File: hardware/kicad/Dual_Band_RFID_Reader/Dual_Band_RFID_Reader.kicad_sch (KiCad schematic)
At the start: 1 part, among them U1 Adafruit_Huzzah32

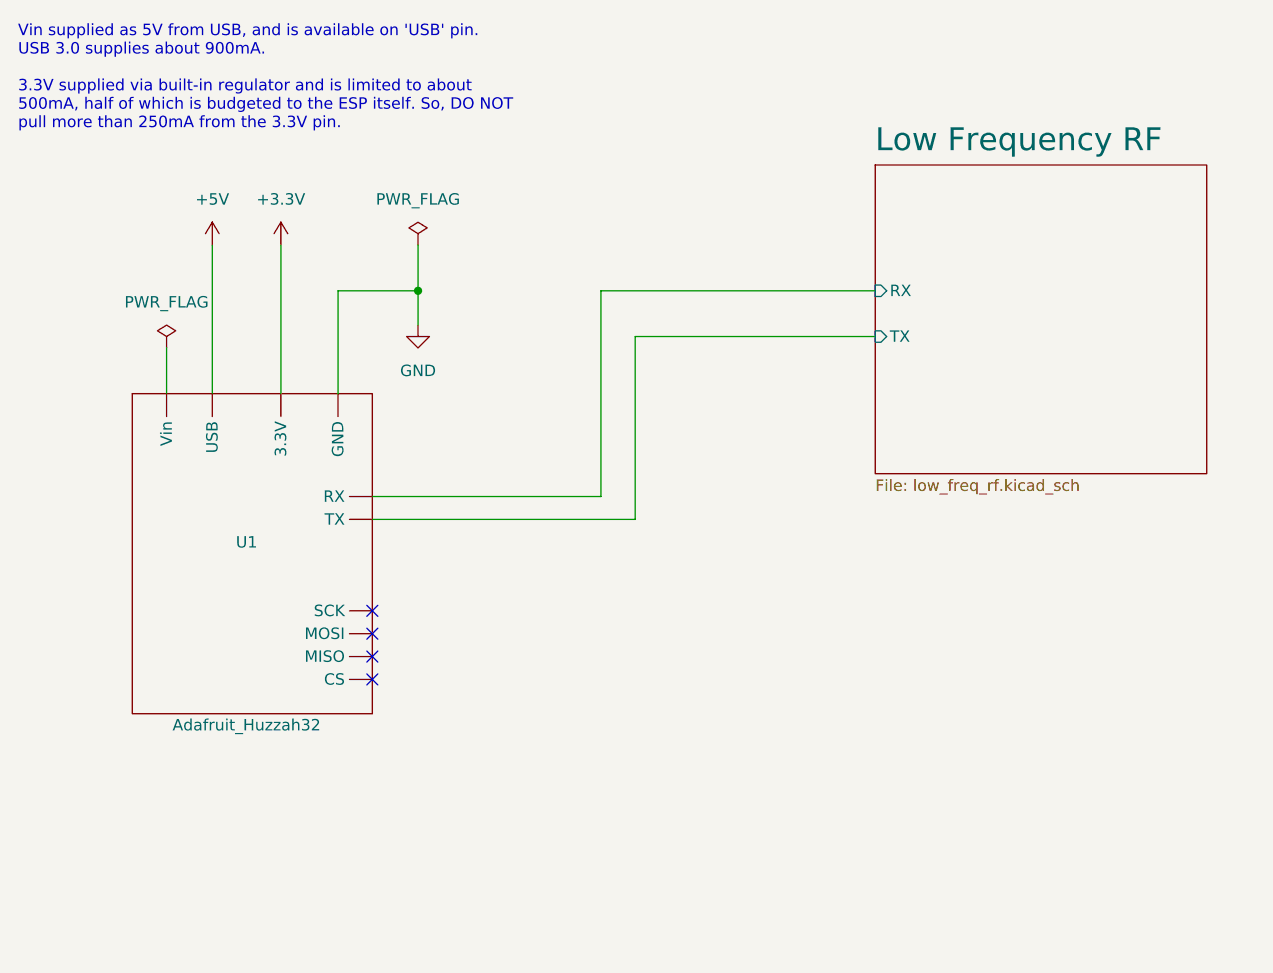
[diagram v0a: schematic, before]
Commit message: First pass at HF and LF schematics
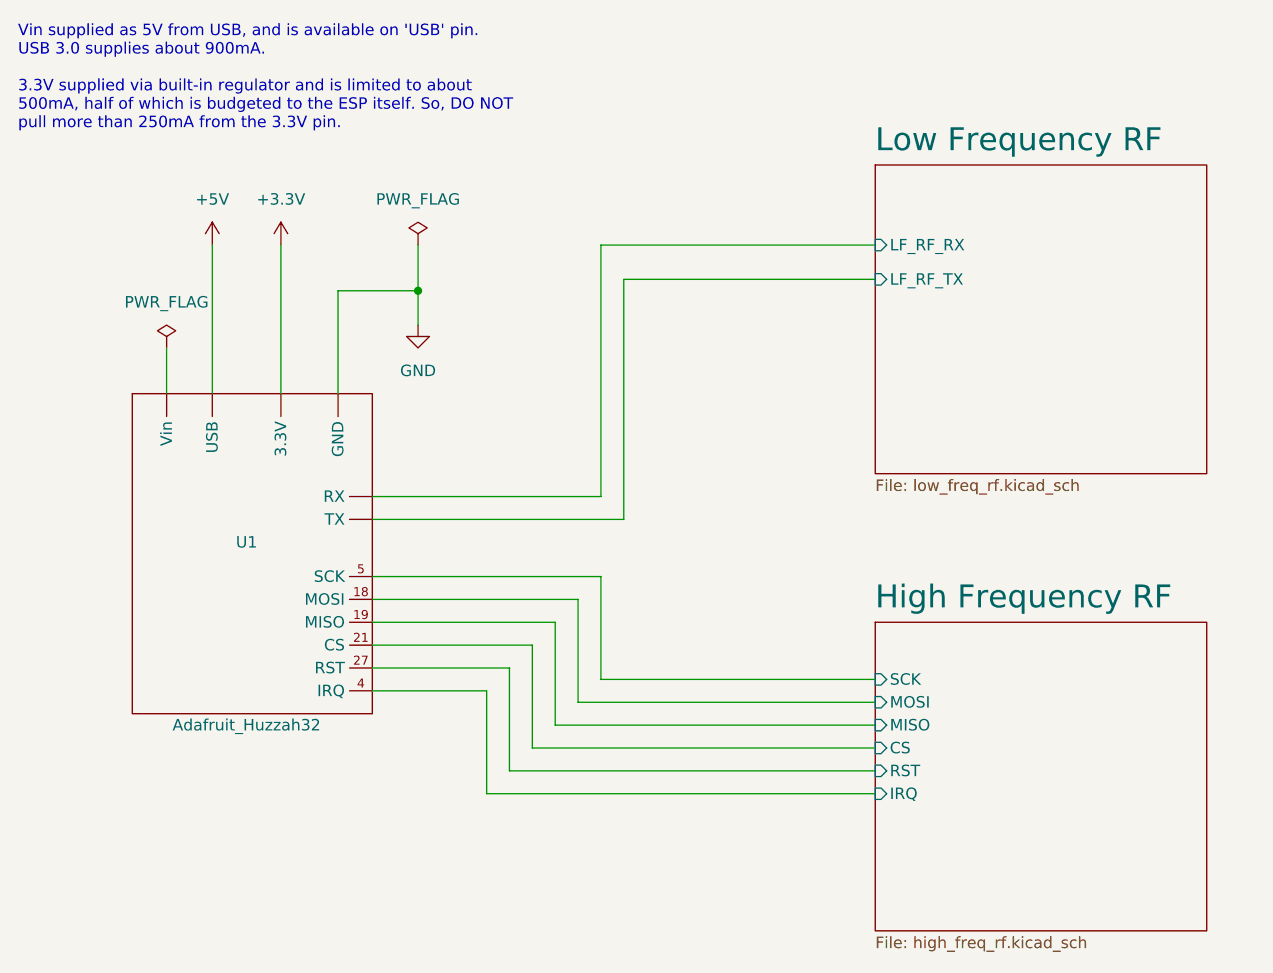
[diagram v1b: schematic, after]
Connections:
- net Low Frequency RF/RX is gone; now on net Low Frequency RF/LF_RF_TX: U1. (Vin)
- net Low Frequency RF/TX is gone; now on net Low Frequency RF/LF_RF_TX: U1. (Vin)
- net Low Frequency RF/LF_RF_TX: now reaches U1. (Vin)
- new net High Frequency RF/CS: U1.21 (CS)
- new net High Frequency RF/IRQ: U1.4 (IRQ)
- new net High Frequency RF/MISO: U1.19 (MISO)
- new net High Frequency RF/MOSI: U1.18 (MOSI)
- new net High Frequency RF/RST: U1.27 (RST)
- new net High Frequency RF/SCK: U1.5 (SCK)
- new net Low Frequency RF/LF_RF_RX: U1. (Vin)
- no-connect marks 4 -> 0
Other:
- added sheet High Frequency RF (high_freq_rf.kicad_sch)
- sheet Low Frequency RF ports: added LF_RF_RX, LF_RF_TX; removed RX, TX

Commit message: Remove IRQ hw line from MFRC522, it's not useful
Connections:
- removed net High Frequency RF/IRQ: U1.4 (IRQ)
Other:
- sheet High Frequency RF ports: added none; removed IRQ
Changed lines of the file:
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@@
-    (stroke (width 0) (type default))
-  )
-  (wire (pts (xy 69.85 125.73) (xy 82.55 125.73))
-    (stroke (width 0) (type default))
-  )
-  (wire (pts (xy 82.55 125.73) (xy 82.55 137.16))
-    (stroke (width 0) (type default))
-  )
-  (wire (pts (xy 82.55 137.16) (xy 125.73 137.16))
     (stroke (width 0) (type default))
   )
@@
     (pin "21")
     (pin "27")
-    (pin "4")
     (pin "5")
   )
@@
       (effects (font (size 1.27 1.27)) (justify left))
     )
-    (pin "IRQ" input (at 125.73 137.16 180)
-      (effects (font (size 1.27 1.27)) (justify left))
-    )

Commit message: adding Mousa's board work to branch
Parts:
- U1: footprint (none) -> Capstone Footprint Lib:Adafruit Feather Huzzah 32; symbol capstone:Adafruit_Huzzah32 -> Capstone Symbol Lib:Adafruit_Huzzah32
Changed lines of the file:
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@@
     (pin "1")
   )
-  (symbol (lib_id "capstone:Adafruit_Huzzah32") (at 55.88 109.22 0) (unit 1)
+  (symbol (lib_id "Capstone Symbol Lib:Adafruit_Huzzah32") (at 55.88 109.22 0) (unit 1)
     (in_bom yes) (on_board yes) (fields_autoplaced)
     (property "Reference" "U1" (id 0) (at 55.88 109.22 0)
@@
       (effects (font (size 1.27 1.27)))
     )
-    (property "Footprint" "" (id 2) (at 55.88 109.22 0)
+    (property "Footprint" "Capstone Footprint Lib:Adafruit Feather Huzzah 32" (id 2) (at 55.88 109.22 0)
       (effects (font (size 1.27 1.27)) hide)
     )
@@
     )
     (path "/2a5888bc-6902-48de-89e6-17a0ce9b4141/5acb20b2-f807-4496-9f75-1929fd1f542d"
-      (reference "D1") (unit 1) (value "1N4148") (footprint "")
+      (reference "D1") (unit 1) (value "1N4148") (footprint "ZenerDiodes:DIOAD829W49L456D191")
     )
     (path "/2a5888bc-6902-48de-89e6-17a0ce9b4141/8a6d9f77-981f-4711-a139-385b0b2abc7c"
@@
     )
     (path "/bc559fd9-5ee4-4aad-844b-eca350a94832/15e8eb38-fa13-4ee5-a10b-52d3c19420ad"
-      (reference "L2") (unit 1) (value "INDUCTOR") (footprint "")
+      (reference "L2") (unit 1) (value "INDUCTOR") (footprint "Inductor_SMD:L_0603_1608Metric_Pad1.05x0.95mm_HandSolder")
     )
     (path "/bc559fd9-5ee4-4aad-844b-eca350a94832/9fe3cc0f-94ef-45c0-99a6-5c285f71f685"
-      (reference "L3") (unit 1) (value "INDUCTOR") (footprint "")
+      (reference "L3") (unit 1) (value "INDUCTOR") (footprint "Inductor_SMD:L_0603_1608Metric_Pad1.05x0.95mm_HandSolder")
     )
     (path "/bc559fd9-5ee4-4aad-844b-eca350a94832/0c00bcad-fbb0-4a8f-8eae-5cacf8dc3091"
-      (reference "L4") (unit 1) (value "INDUCTOR") (footprint "")
+      (reference "L4") (unit 1) (value "INDUCTOR") (footprint "Inductor_SMD:L_0603_1608Metric_Pad1.05x0.95mm_HandSolder")
     )
     (path "/2a5888bc-6902-48de-89e6-17a0ce9b4141/a2af022a-47d0-4ef8-8e55-89cd26190f9b"
@@
     )
     (path "/eeb3eed9-254a-481d-a4b3-7177dae5988c"
-      (reference "U1") (unit 1) (value "Adafruit_Huzzah32") (footprint "")
+      (reference "U1") (unit 1) (value "Adafruit_Huzzah32") (footprint "Capstone Footprint Lib:Adafruit Feather Huzzah 32")
     )
     (path "/2a5888bc-6902-48de-89e6-17a0ce9b4141/4ac97269-7e37-4137-bb95-a31528674e8f"
-      (reference "U2") (unit 1) (value "LM393") (footprint "")
+      (reference "U2") (unit 1) (value "LM393") (footprint "DualComparator_LM393:SO08")
     )
     (path "/2a5888bc-6902-48de-89e6-17a0ce9b4141/8f68e74a-7b7b-4ea1-9129-44a724df83ae"
-      (reference "U3") (unit 1) (value "LM324") (footprint "")
+      (reference "U3") (unit 1) (value "LM324") (footprint "GPOPAmp_LM324:SOIC127P600X175-14N")
     )
     (path "/bc559fd9-5ee4-4aad-844b-eca350a94832/87de0e83-a3b8-45fc-9ed8-06568275cf07"
-      (reference "U4") (unit 1) (value "MFRC522") (footprint "")
+      (reference "U4") (unit 1) (value "MFRC522") (footprint "MIFARE:QFN50P500X500X100-33N")
     )
     (path "/bc559fd9-5ee4-4aad-844b-eca350a94832/190d7b3a-0eea-4cf5-b0a2-3e98dee623a4"
-      (reference "Y1") (unit 1) (value "Crystal") (footprint "")
-    )
-  )
+      (reference "Y1") (unit 1) (value "Crystal") (footprint "Capstone Footprint Lib:Crystal_SMD_3225-4Pin_3.2x2.5mm_HandSoldering")
+    )
+  )

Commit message: Board Layout WIP
* Added correct footprint for the components that were
  producing errors
* added HF antenna trace on board periphery
* added pads for the LF antenna coil to be connected later
* corrected all the DRC errors
* completed HF layout
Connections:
- net +3V3: now also U1.2 (3.3V); no longer U1. (Vin)
- net +5V: now also U1.26 (USB); no longer U1. (Vin)
- net GND: now also U1.4 (GND); no longer U1. (Vin)
- net High Frequency RF/CS: now also U1.16 (CS); no longer U1.21 (CS)
- net High Frequency RF/MISO: now also U1.13 (MISO); no longer U1.19 (MISO)
- net High Frequency RF/MOSI: now also U1.12 (MOSI); no longer U1.18 (MOSI)
- net High Frequency RF/RST: now also U1.23 (RST); no longer U1.27 (RST)
- net High Frequency RF/SCK: now also U1.11 (SCK); no longer U1.5 (SCK)
- net Low Frequency RF/LF_RF_RX: now also U1.14 (RX); no longer U1. (Vin)
- net Low Frequency RF/LF_RF_TX: now also U1.15 (TX); no longer U1. (Vin)
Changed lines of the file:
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@@
     )
     (pin "")
-    (pin "")
-    (pin "")
-    (pin "")
-    (pin "")
-    (pin "")
-    (pin "18")
-    (pin "19")
-    (pin "21")
-    (pin "27")
-    (pin "5")
+    (pin "11")
+    (pin "12")
+    (pin "13")
+    (pin "14")
+    (pin "15")
+    (pin "16")
+    (pin "2")
+    (pin "23")
+    (pin "26")
+    (pin "4")
   )
   (sheet (at 125.73 67.31) (size 36.83 34.29) (fields_autoplaced)
@@
     )
     (path "/2a5888bc-6902-48de-89e6-17a0ce9b4141/5acb20b2-f807-4496-9f75-1929fd1f542d"
-      (reference "D1") (unit 1) (value "1N4148") (footprint "ZenerDiodes:DIOAD829W49L456D191")
+      (reference "D1") (unit 1) (value "1N4148") (footprint "Diode_SMD:D_SOD-123")
     )
     (path "/2a5888bc-6902-48de-89e6-17a0ce9b4141/8a6d9f77-981f-4711-a139-385b0b2abc7c"
-      (reference "L1") (unit 1) (value "162 µH") (footprint "")
+      (reference "L1") (unit 1) (value "162 µH") (footprint "Capstone Footprint Lib:LF Antenna Pads")
     )
     (path "/bc559fd9-5ee4-4aad-844b-eca350a94832/15e8eb38-fa13-4ee5-a10b-52d3c19420ad"
-      (reference "L2") (unit 1) (value "INDUCTOR") (footprint "Inductor_SMD:L_0603_1608Metric_Pad1.05x0.95mm_HandSolder")
+      (reference "L2") (unit 1) (value "INDUCTOR") (footprint "Inductor_SMD:L_1210_3225Metric_Pad1.42x2.65mm_HandSolder")
     )
     (path "/bc559fd9-5ee4-4aad-844b-eca350a94832/9fe3cc0f-94ef-45c0-99a6-5c285f71f685"
-      (reference "L3") (unit 1) (value "INDUCTOR") (footprint "Inductor_SMD:L_0603_1608Metric_Pad1.05x0.95mm_HandSolder")
-    )
-    (path "/bc559fd9-5ee4-4aad-844b-eca350a94832/0c00bcad-fbb0-4a8f-8eae-5cacf8dc3091"
-      (reference "L4") (unit 1) (value "INDUCTOR") (footprint "Inductor_SMD:L_0603_1608Metric_Pad1.05x0.95mm_HandSolder")
+      (reference "L3") (unit 1) (value "INDUCTOR") (footprint "Inductor_SMD:L_1210_3225Metric_Pad1.42x2.65mm_HandSolder")
     )
     (path "/2a5888bc-6902-48de-89e6-17a0ce9b4141/a2af022a-47d0-4ef8-8e55-89cd26190f9b"
-      (reference "Q1") (unit 1) (value "BC517") (footprint "Package_TO_SOT_THT:TO-92_Inline")
+      (reference "Q1") (unit 1) (value "BC517") (footprint "Package_TO_SOT_SMD:SOT-223")
     )
     (path "/2a5888bc-6902-48de-89e6-17a0ce9b4141/455ff276-4778-486d-9b03-8a3b3124665a"
@@
     )
     (path "/2a5888bc-6902-48de-89e6-17a0ce9b4141/4ac97269-7e37-4137-bb95-a31528674e8f"
-      (reference "U2") (unit 1) (value "LM393") (footprint "DualComparator_LM393:SO08")
+      (reference "U2") (unit 1) (value "LM393") (footprint "Package_SO:SOIC-8_3.9x4.9mm_P1.27mm")
     )
     (path "/2a5888bc-6902-48de-89e6-17a0ce9b4141/8f68e74a-7b7b-4ea1-9129-44a724df83ae"
-      (reference "U3") (unit 1) (value "LM324") (footprint "GPOPAmp_LM324:SOIC127P600X175-14N")
+      (reference "U3") (unit 1) (value "LM324") (footprint "Package_SO:SOIC-14_3.9x8.7mm_P1.27mm")
     )
     (path "/bc559fd9-5ee4-4aad-844b-eca350a94832/87de0e83-a3b8-45fc-9ed8-06568275cf07"
-      (reference "U4") (unit 1) (value "MFRC522") (footprint "MIFARE:QFN50P500X500X100-33N")
+      (reference "U4") (unit 1) (value "MFRC522") (footprint "Package_DFN_QFN:QFN-32-1EP_5x5mm_P0.5mm_EP3.3x3.3mm")
     )
     (path "/bc559fd9-5ee4-4aad-844b-eca350a94832/190d7b3a-0eea-4cf5-b0a2-3e98dee623a4"

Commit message: Updates traces
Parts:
- U1: footprint Capstone Footprint Lib:Adafruit Feather Huzzah 32 -> Module:Adafruit_Feather_WithMountingHoles; symbol Capstone Symbol Lib:Adafruit_Huzzah32 -> capstone:Adafruit_Huzzah32
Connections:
- net +3V3: now also U1. (Vin); no longer U1.2 (3.3V)
- net +5V: now also U1. (Vin); no longer U1.26 (USB)
- net GND: now also U1. (Vin); no longer U1.4 (GND)
- net High Frequency RF/CS: now also U1.21 (CS); no longer U1.16 (CS)
- net High Frequency RF/MISO: now also U1.19 (MISO); no longer U1.13 (MISO)
- net High Frequency RF/MOSI: now also U1.18 (MOSI); no longer U1.12 (MOSI)
- net High Frequency RF/RST: now also U1.27 (RST); no longer U1.23 (RST)
- net High Frequency RF/SCK: now also U1.5 (SCK); no longer U1.11 (SCK)
- net Low Frequency RF/LF_RF_RX: now also U1. (Vin); no longer U1.14 (RX)
- net Low Frequency RF/LF_RF_TX: now also U1. (Vin); no longer U1.15 (TX)
- new net High Frequency RF/IRQ: U1.4 (IRQ)
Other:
- sheet High Frequency RF ports: added IRQ; removed none
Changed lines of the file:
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@@
+    (stroke (width 0) (type default))
+  )
+  (wire (pts (xy 69.85 125.73) (xy 82.55 125.73))
+    (stroke (width 0) (type default))
+  )
+  (wire (pts (xy 82.55 125.73) (xy 82.55 137.16))
+    (stroke (width 0) (type default))
+  )
+  (wire (pts (xy 82.55 137.16) (xy 125.73 137.16))
     (stroke (width 0) (type default))
   )
@@
     (pin "1")
   )
-  (symbol (lib_id "Capstone Symbol Lib:Adafruit_Huzzah32") (at 55.88 109.22 0) (unit 1)
+  (symbol (lib_id "capstone:Adafruit_Huzzah32") (at 55.88 109.22 0) (unit 1)
     (in_bom yes) (on_board yes) (fields_autoplaced)
     (property "Reference" "U1" (id 0) (at 55.88 109.22 0)
@@
       (effects (font (size 1.27 1.27)))
     )
-    (property "Footprint" "Capstone Footprint Lib:Adafruit Feather Huzzah 32" (id 2) (at 55.88 109.22 0)
+    (property "Footprint" "Module:Adafruit_Feather_WithMountingHoles" (id 2) (at 55.88 109.22 0)
       (effects (font (size 1.27 1.27)) hide)
     )
@@
     )
     (pin "")
-    (pin "11")
-    (pin "12")
-    (pin "13")
-    (pin "14")
-    (pin "15")
-    (pin "16")
-    (pin "2")
-    (pin "23")
-    (pin "26")
+    (pin "")
+    (pin "")
+    (pin "")
+    (pin "")
+    (pin "")
+    (pin "18")
+    (pin "19")
+    (pin "21")
+    (pin "27")
     (pin "4")
+    (pin "5")
   )
   (sheet (at 125.73 67.31) (size 36.83 34.29) (fields_autoplaced)
@@
       (effects (font (size 1.27 1.27)) (justify left))
     )
+    (pin "IRQ" input (at 125.73 137.16 180)
+      (effects (font (size 1.27 1.27)) (justify left))
+    )
     (pin "CS" input (at 125.73 132.08 180)
       (effects (font (size 1.27 1.27)) (justify left))
@@
     )
     (path "/2a5888bc-6902-48de-89e6-17a0ce9b4141/5acb20b2-f807-4496-9f75-1929fd1f542d"
-      (reference "D1") (unit 1) (value "1N4148") (footprint "Diode_SMD:D_SOD-123")
+      (reference "D1") (unit 1) (value "1N4148") (footprint "ZenerDiodes:DIOAD829W49L456D191")
     )
     (path "/2a5888bc-6902-48de-89e6-17a0ce9b4141/8a6d9f77-981f-4711-a139-385b0b2abc7c"
-      (reference "L1") (unit 1) (value "162 µH") (footprint "Capstone Footprint Lib:LF Antenna Pads")
+      (reference "L1") (unit 1) (value "162 µH") (footprint "")
     )
     (path "/bc559fd9-5ee4-4aad-844b-eca350a94832/15e8eb38-fa13-4ee5-a10b-52d3c19420ad"
-      (reference "L2") (unit 1) (value "INDUCTOR") (footprint "Inductor_SMD:L_1210_3225Metric_Pad1.42x2.65mm_HandSolder")
+      (reference "L2") (unit 1) (value "INDUCTOR") (footprint "Inductor_SMD:L_0603_1608Metric_Pad1.05x0.95mm_HandSolder")
     )
     (path "/bc559fd9-5ee4-4aad-844b-eca350a94832/9fe3cc0f-94ef-45c0-99a6-5c285f71f685"
-      (reference "L3") (unit 1) (value "INDUCTOR") (footprint "Inductor_SMD:L_1210_3225Metric_Pad1.42x2.65mm_HandSolder")
+      (reference "L3") (unit 1) (value "INDUCTOR") (footprint "Inductor_SMD:L_0603_1608Metric_Pad1.05x0.95mm_HandSolder")
+    )
+    (path "/bc559fd9-5ee4-4aad-844b-eca350a94832/0c00bcad-fbb0-4a8f-8eae-5cacf8dc3091"
+      (reference "L4") (unit 1) (value "INDUCTOR") (footprint "Inductor_SMD:L_0603_1608Metric_Pad1.05x0.95mm_HandSolder")
     )
     (path "/2a5888bc-6902-48de-89e6-17a0ce9b4141/a2af022a-47d0-4ef8-8e55-89cd26190f9b"
-      (reference "Q1") (unit 1) (value "BC517") (footprint "Package_TO_SOT_SMD:SOT-223")
+      (reference "Q1") (unit 1) (value "BC517") (footprint "Package_TO_SOT_THT:TO-92_Inline")
     )
     (path "/2a5888bc-6902-48de-89e6-17a0ce9b4141/455ff276-4778-486d-9b03-8a3b3124665a"
@@
     )
     (path "/eeb3eed9-254a-481d-a4b3-7177dae5988c"
-      (reference "U1") (unit 1) (value "Adafruit_Huzzah32") (footprint "Capstone Footprint Lib:Adafruit Feather Huzzah 32")
+      (reference "U1") (unit 1) (value "Adafruit_Huzzah32") (footprint "Module:Adafruit_Feather_WithMountingHoles")
     )
     (path "/2a5888bc-6902-48de-89e6-17a0ce9b4141/4ac97269-7e37-4137-bb95-a31528674e8f"
-      (reference "U2") (unit 1) (value "LM393") (footprint "Package_SO:SOIC-8_3.9x4.9mm_P1.27mm")
+      (reference "U2") (unit 1) (value "LM393") (footprint "DualComparator_LM393:SO08")
     )
     (path "/2a5888bc-6902-48de-89e6-17a0ce9b4141/8f68e74a-7b7b-4ea1-9129-44a724df83ae"
-      (reference "U3") (unit 1) (value "LM324") (footprint "Package_SO:SOIC-14_3.9x8.7mm_P1.27mm")
+      (reference "U3") (unit 1) (value "LM324") (footprint "GPOPAmp_LM324:SOIC127P600X175-14N")
     )
     (path "/bc559fd9-5ee4-4aad-844b-eca350a94832/87de0e83-a3b8-45fc-9ed8-06568275cf07"
-      (reference "U4") (unit 1) (value "MFRC522") (footprint "Package_DFN_QFN:QFN-32-1EP_5x5mm_P0.5mm_EP3.3x3.3mm")
+      (reference "U4") (unit 1) (value "MFRC522") (footprint "MIFARE:QFN50P500X500X100-33N")
     )
     (path "/bc559fd9-5ee4-4aad-844b-eca350a94832/190d7b3a-0eea-4cf5-b0a2-3e98dee623a4"
-      (reference "Y1") (unit 1) (value "Crystal") (footprint "Capstone Footprint Lib:Crystal_SMD_3225-4Pin_3.2x2.5mm_HandSoldering")
-    )
-  )
+      (reference "Y1") (unit 1) (value "Crystal") (footprint "Crystal:Crystal_SMD_HC49-SD_HandSoldering")
+    )
+  )
